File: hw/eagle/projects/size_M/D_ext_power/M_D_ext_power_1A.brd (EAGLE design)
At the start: 21 parts

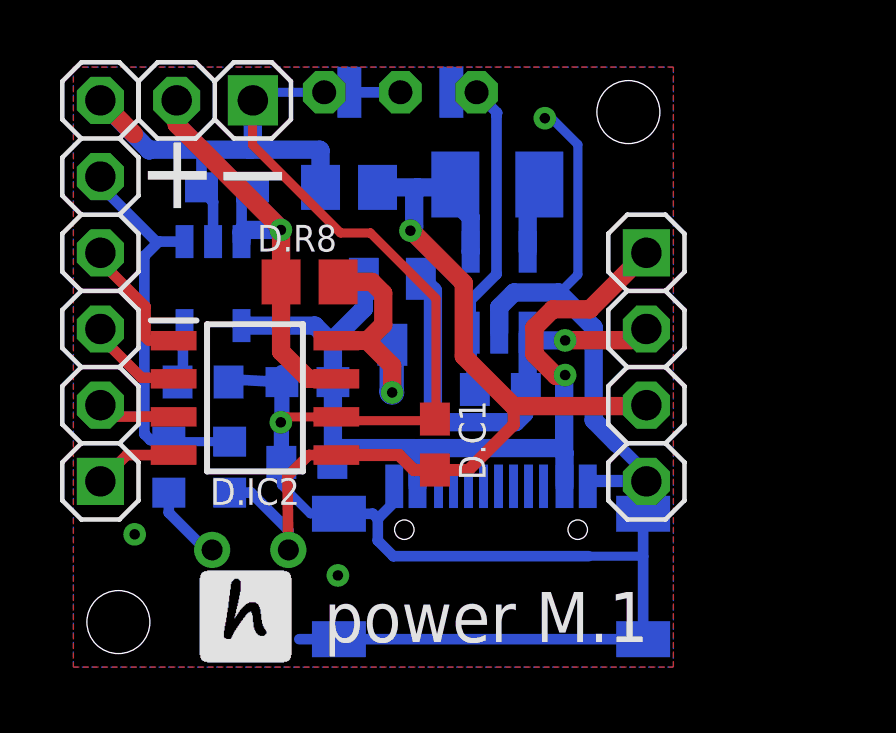
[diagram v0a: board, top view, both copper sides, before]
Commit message: updateed PCBs - adjustments based on usage of version 1
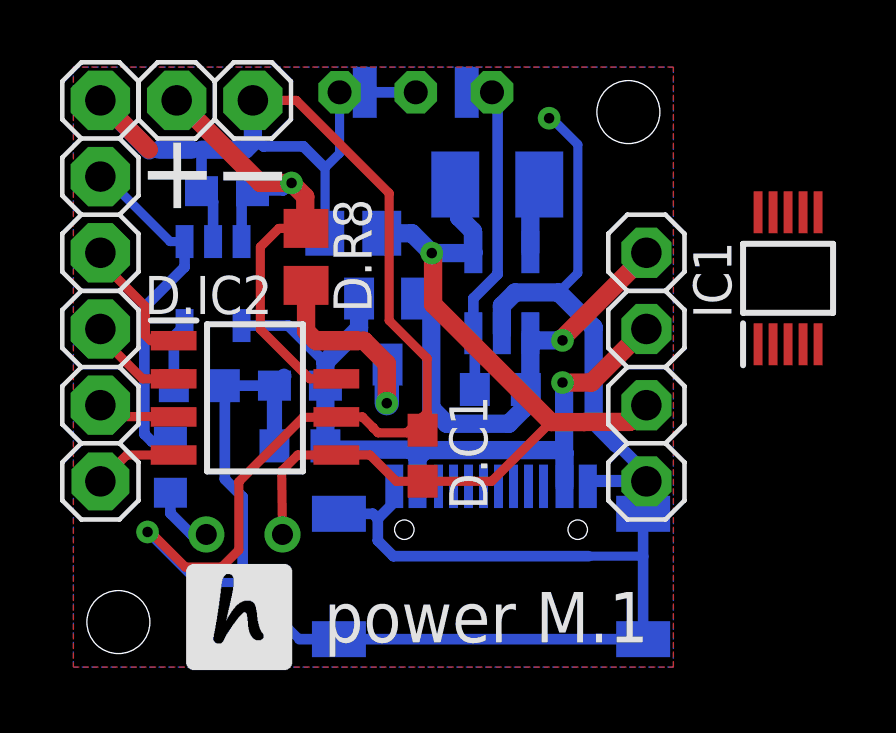
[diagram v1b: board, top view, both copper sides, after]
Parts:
- removed D.R1: 100k, rcl:R0603
- added IC1: MCP73833-AMI_UN, SamacSys_Parts:SOP50P490X110-10N
- moved D.C7 1.54 mm to (9.83, 15.0)
- moved D.R8 0.84 mm to (8.26, 14.2), turned to 90 degrees
- moved D.T1 0.68 mm to (11.0, 11.7)
- moved D.R4 0.60 mm to (8.05, 7.87)
- moved D.C1 0.55 mm to (12.1, 7.54)
- moved D.D1 0.55 mm to (6.20, 4.52)
- moved D.ON/OFF/RESET 0.51 mm to (11.9, 19.7)
- moved D.C4 0.28 mm to (8.05, 9.88)
- moved D.R3 0.17 mm to (4.70, 9.88)
- moved D.C6 0.12 mm to (5.62, 16.4)
- moved D.U2 0.09 mm to (14.8, 13.0)
- moved D.R6 0.05 mm to (3.73, 7.16)
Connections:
- net P0 renamed N$1
- net P1 renamed N$10
- net SCL renamed N$6
- net SDA renamed N$7
- removed net P4: D.J2.5, D.R1.2, D.R6.1, D.U1.1
- new net PA7: D.J2.5, D.R6.1, D.U1.1
- net N$12: now also D.J3.1; no longer D.J3.2
- net N$9: now also D.J3.2; no longer D.J3.1
- net VDD: no longer D.R1.1
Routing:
- net GND: track 99.6 -> 118.7 mm, vias 4 -> 2
- net P4: track 14.6 -> 0.00 mm
- net PA7: track 0.00 -> 11.9 mm
- net N$9: track 33.0 -> 27.1 mm
- net VDD: track 34.2 -> 29.9 mm
- net N$13: track 16.0 -> 17.7 mm
- net N$8: track 9.31 -> 7.82 mm
